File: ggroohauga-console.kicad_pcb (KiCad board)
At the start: 2 copper layers, 95 x 31 mm, 7 parts

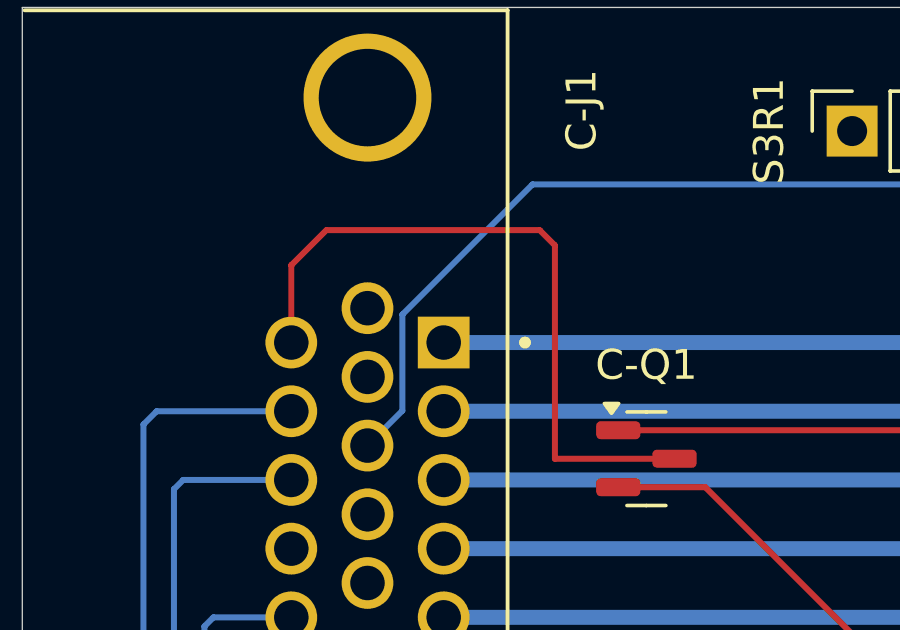
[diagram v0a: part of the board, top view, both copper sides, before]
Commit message: Add 3D models of the DE-15 connectors and realign some tracks
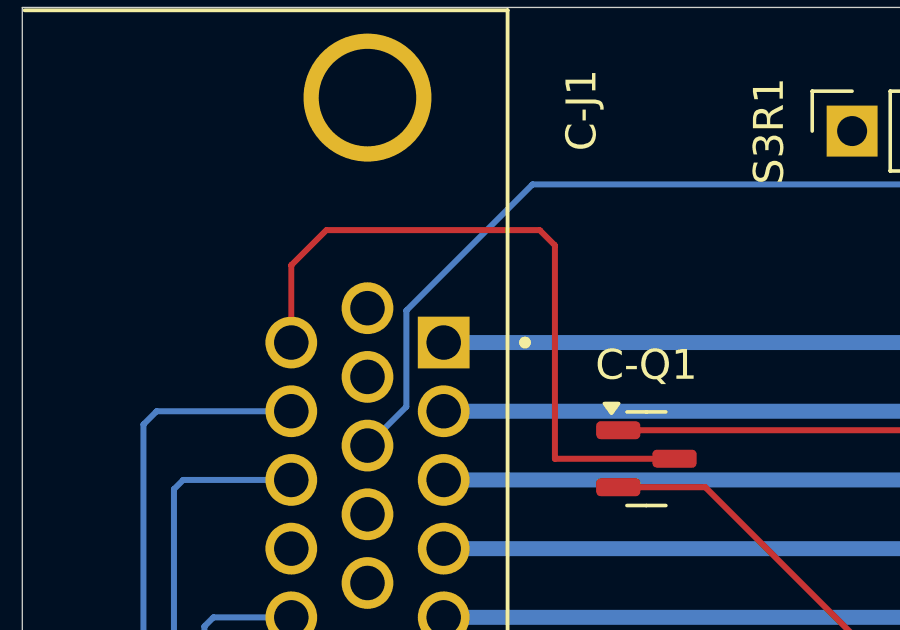
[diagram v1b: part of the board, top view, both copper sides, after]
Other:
- board text added: "urn:oid:1.3.6.1.4.1.39777.1.3.1.2.4"
- board text removed: "urn:oid:1.3.6.1.4.1.39777.1.3.1.2.3"
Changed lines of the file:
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@@
 		)
 		(embedded_fonts no)
+		(model "${KIPRJMOD}/vendor/amphenol/L717HDE15PD1CH4F.step"
+			(offset
+				(xyz 0 -8.5 6.25)
+			)
+			(scale
+				(xyz 1 1 1)
+			)
+			(rotate
+				(xyz -180 -0 -0)
+			)
+		)
 	)
 	(footprint "Connector_PinSocket_2.54mm:PinSocket_1x20_P2.54mm_Vertical"
@@
 		)
 	)
-	(gr_text "urn:oid:1.3.6.1.4.1.39777.1.3.1.2.3"
+	(gr_text "urn:oid:1.3.6.1.4.1.39777.1.3.1.2.4"
 		(at 131.064 56.642 0)
 		(layer "B.SilkS")
@@
 	)
 	(segment
-		(start 120.396 56.388)
-		(end 122.174 54.61)
+		(start 66.675 60.59325)
+		(end 70.88025 56.388)
 		(width 0.2)
 		(layer "B.Cu")
@@
 	)
 	(segment
-		(start 66.5421 63.9317)
-		(end 66.5421 60.72615)
+		(start 66.675 63.7988)
+		(end 66.675 60.59325)
 		(width 0.2)
 		(layer "B.Cu")
@@
 	)
 	(segment
-		(start 65.3796 65.0942)
-		(end 66.5421 63.9317)
+		(start 120.396 56.388)
+		(end 122.174 54.61)
 		(width 0.2)
 		(layer "B.Cu")
@@
 	)
 	(segment
-		(start 66.5421 60.72615)
-		(end 70.88025 56.388)
+		(start 65.3796 65.0942)
+		(end 66.675 63.7988)
 		(width 0.2)
 		(layer "B.Cu")

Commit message: Indicate active low signals on the schematic
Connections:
- net /Common/GPIO_L13_C47_M26/AMP_ANNOUNCE renamed /Common/~{GPIO_L13_C47_M26/AMP_ANNOUNCE}
- net /Common/GPIO_L17_C17_M8/CON_DETECT renamed /Common/~{GPIO_L17_C17_M8/CON_DETECT}
- net /Common/GPIO_L21_C21_M21/AMP_DETECT renamed /Common/~{GPIO_L21_C21_M21/AMP_DETECT}
- net /Common/GPIO_L40_C40_M41/CON_POWER_OUT renamed /Common/~{GPIO_L40_C40_M41/CON_POWER_OUT}
- net /Common/GPIO_L41_C41_M42/CON_ANNOUNCE renamed /Common/~{GPIO_L41_C41_M42/CON_ANNOUNCE}

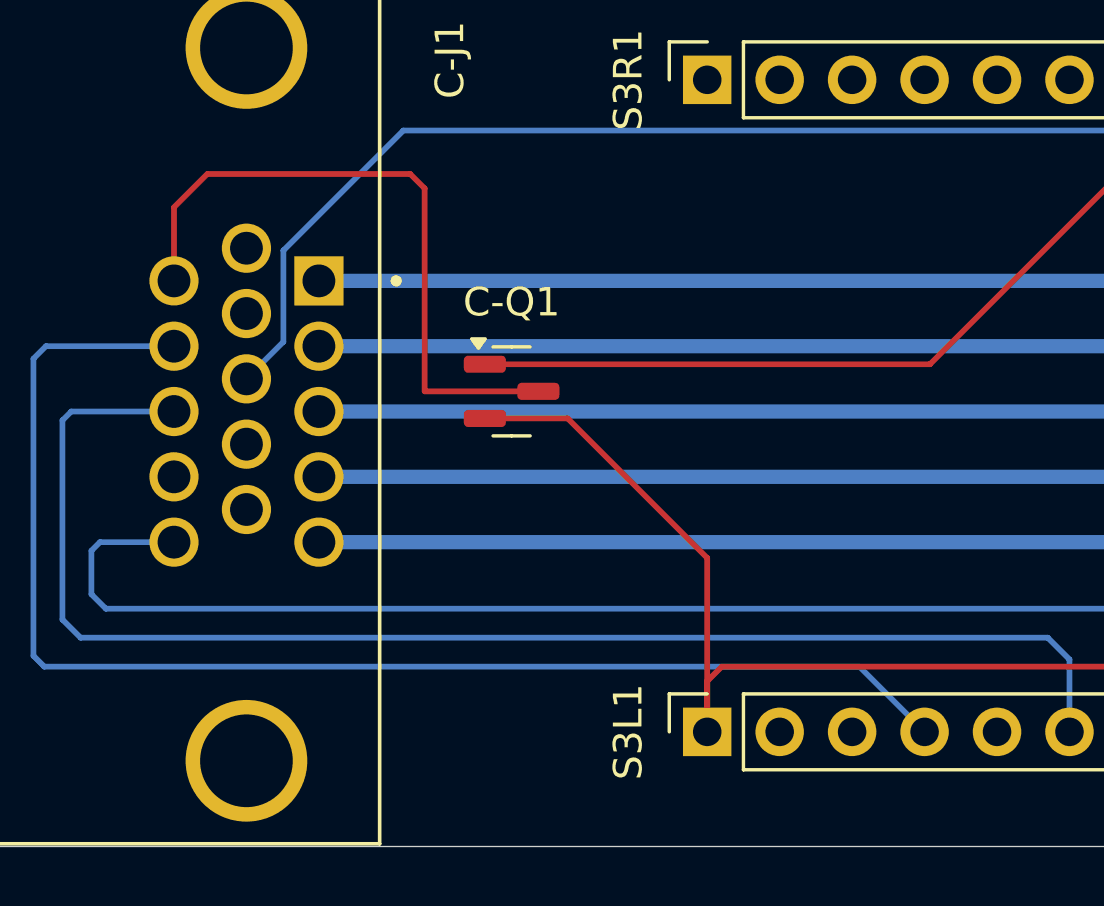
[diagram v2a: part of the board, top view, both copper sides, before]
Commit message: Use the better SOT-23-3 footprint for C-Q1
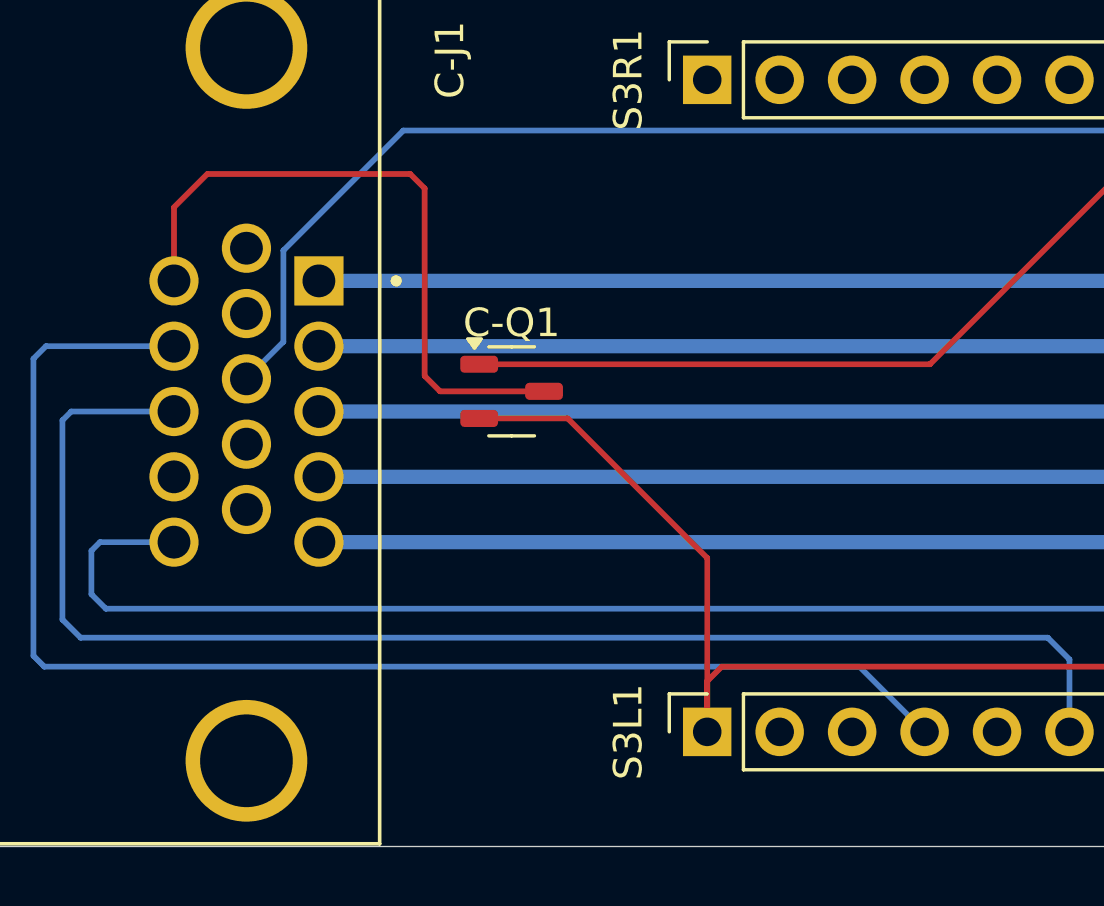
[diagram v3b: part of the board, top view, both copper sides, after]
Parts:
- C-Q1: footprint Package_TO_SOT_SMD:SOT-23 -> Package_TO_SOT_SMD:SOT-23-3
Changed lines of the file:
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@@
 	(net 42 "/Common/~{GPIO_L17_C17_M8{slash}CON_DETECT}")
 	(net 43 "/Common/~{GPIO_L40_C40_M41{slash}CON_POWER_OUT}")
-	(footprint "Package_TO_SOT_SMD:SOT-23"
+	(footprint "Package_TO_SOT_SMD:SOT-23-3"
 		(layer "F.Cu")
 		(at 74.676 65.532)
-		(descr "SOT, 3 Pin (JEDEC TO-236 Var AB https://www.jedec.org/document_search?search_api_views_fulltext=TO-236), generated with kicad-footprint-generator ipc_gullwing_generator.py")
+		(descr "SOT, 3 Pin (JEDEC MO-178 inferred 3-pin variant https://www.jedec.org/document_search?search_api_views_fulltext=MO-178), generated with kicad-footprint-generator ipc_gullwing_generator.py")
 		(tags "SOT TO_SOT_SMD")
 		(property "Reference" "C-Q1"
-			(at 0 -3.1265 0)
+			(at 0 -2.4 0)
 			(layer "F.SilkS")
 			(effects
@@
 		(fp_line
 			(start 0 -1.56)
-			(end -0.65 -1.56)
+			(end -0.8 -1.56)
 			(stroke
 				(width 0.12)
@@
 		(fp_line
 			(start 0 -1.56)
-			(end 0.65 -1.56)
+			(end 0.8 -1.56)
 			(stroke
 				(width 0.12)
@@
 		(fp_line
 			(start 0 1.56)
-			(end -0.65 1.56)
+			(end -0.8 1.56)
 			(stroke
 				(width 0.12)
@@
 		(fp_line
 			(start 0 1.56)
-			(end 0.65 1.56)
+			(end 0.8 1.56)
 			(stroke
 				(width 0.12)
@@
 		(fp_poly
 			(pts
-				(xy -1.1625 -1.51) (xy -1.4025 -1.84) (xy -0.9225 -1.84)
+				(xy -1.3 -1.51) (xy -1.54 -1.84) (xy -1.06 -1.84)
 			)
 			(stroke
@@
 		)
 		(fp_line
-			(start -1.93 -1.5)
-			(end -0.9 -1.5)
+			(start -2.05 -1.5)
+			(end -1.05 -1.5)
 			(stroke
 				(width 0.05)
@@
 		)
 		(fp_line
-			(start -1.93 1.5)
-			(end -1.93 -1.5)
+			(start -2.05 1.5)
+			(end -2.05 -1.5)
 			(stroke
 				(width 0.05)
@@
 		)
 		(fp_line
-			(start -0.9 -1.7)
-			(end 0.9 -1.7)
+			(start -1.05 -1.7)
+			(end 1.05 -1.7)
 			(stroke
 				(width 0.05)
@@
 		)
 		(fp_line
-			(start -0.9 -1.5)
-			(end -0.9 -1.7)
+			(start -1.05 -1.5)
+			(end -1.05 -1.7)
 			(stroke
 				(width 0.05)
@@
 		)
 		(fp_line
-			(start -0.9 1.5)
-			(end -1.93 1.5)
+			(start -1.05 1.5)
+			(end -2.05 1.5)
 			(stroke
 				(width 0.05)
@@
 		)
 		(fp_line
-			(start -0.9 1.7)
-			(end -0.9 1.5)
+			(start -1.05 1.7)
+			(end -1.05 1.5)
 			(stroke
 				(width 0.05)
@@
 		)
 		(fp_line
-			(start 0.9 -1.7)
-			(end 0.9 -0.55)
+			(start 1.05 -1.7)
+			(end 1.05 -0.55)
 			(stroke
 				(width 0.05)
@@
 		)
 		(fp_line
-			(start 0.9 -0.55)
-			(end 1.93 -0.55)
+			(start 1.05 -0.55)
+			(end 2.05 -0.55)
 			(stroke
 				(width 0.05)
@@
 		)
 		(fp_line
-			(start 0.9 0.55)
-			(end 0.9 1.7)
+			(start 1.05 0.55)
+			(end 1.05 1.7)
 			(stroke
 				(width 0.05)
@@
 		)
 		(fp_line
-			(start 0.9 1.7)
-			(end -0.9 1.7)
+			(start 1.05 1.7)
+			(end -1.05 1.7)
 			(stroke
 				(width 0.05)
@@
 		)
 		(fp_line
-			(start 1.93 -0.55)
-			(end 1.93 0.55)
+			(start 2.05 -0.55)
+			(end 2.05 0.55)
 			(stroke
 				(width 0.05)
@@
 		)
 		(fp_line
-			(start 1.93 0.55)
-			(end 0.9 0.55)
+			(start 2.05 0.55)
+			(end 1.05 0.55)
 			(stroke
 				(width 0.05)
@@
 		)
 		(fp_line
-			(start -0.65 -1.125)
-			(end -0.325 -1.45)
+			(start -0.8 -1.05)
+			(end -0.4 -1.45)
 			(stroke
 				(width 0.1)
@@
 		)
 		(fp_line
-			(start -0.65 1.45)
-			(end -0.65 -1.125)
+			(start -0.8 1.45)
+			(end -0.8 -1.05)
 			(stroke
 				(width 0.1)
@@
 		)
 		(fp_line
-			(start -0.325 -1.45)
-			(end 0.65 -1.45)
+			(start -0.4 -1.45)
+			(end 0.8 -1.45)
 			(stroke
 				(width 0.1)
@@
 		)
 		(fp_line
-			(start 0.65 -1.45)
-			(end 0.65 1.45)
+			(start 0.8 -1.45)
+			(end 0.8 1.45)
 			(stroke
 				(width 0.1)
@@
 		)
 		(fp_line
-			(start 0.65 1.45)
-			(end -0.65 1.45)
+			(start 0.8 1.45)
+			(end -0.8 1.45)
 			(stroke
 				(width 0.1)
@@
 			(effects
 				(font
-					(size 0.32 0.32)
-					(thickness 0.05)
+					(size 0.4 0.4)
+					(thickness 0.06)
 				)
 			)
 		)
 		(pad "1" smd roundrect
-			(at -0.9375 -0.95)
-			(size 1.475 0.6)
+			(at -1.1375 -0.95)
+			(size 1.325 0.6)
 			(layers "F.Cu" "F.Mask" "F.Paste")
 			(roundrect_rratio 0.25)
@@
 		)
 		(pad "2" smd roundrect
-			(at -0.9375 0.95)
-			(size 1.475 0.6)
+			(at -1.1375 0.95)
+			(size 1.325 0.6)
 			(layers "F.Cu" "F.Mask" "F.Paste")
 			(roundrect_rratio 0.25)
@@
 		)
 		(pad "3" smd roundrect
-			(at 0.9375 0)
-			(size 1.475 0.6)
+			(at 1.1375 0)
+			(size 1.325 0.6)
 			(layers "F.Cu" "F.Mask" "F.Paste")
 			(roundrect_rratio 0.25)
@@
 		)
 		(embedded_fonts no)
-		(model "${KICAD9_3DMODEL_DIR}/Package_TO_SOT_SMD.3dshapes/SOT-23.step"
+		(model "${KICAD9_3DMODEL_DIR}/Package_TO_SOT_SMD.3dshapes/SOT-23-3.step"
 			(offset
 				(xyz 0 0 0)
@@
 	)
 	(segment
+		(start 73.5385 66.482)
+		(end 76.642 66.482)
+		(width 0.2)
+		(layer "F.Cu")
+		(net 8)
+	)
+	(segment
 		(start 76.642 66.482)
 		(end 81.534 71.374)
@@
 	)
 	(segment
-		(start 81.534 77.47)
-		(end 81.534 71.374)
-		(width 0.2)
-		(layer "F.Cu")
-		(net 8)
-	)
-	(segment
-		(start 73.7385 66.482)
-		(end 76.642 66.482)
+		(start 82.042 75.184)
+		(end 81.534 75.692)
 		(width 0.2)
 		(layer "F.Cu")
@@
 	)
 	(segment
-		(start 82.042 75.184)
-		(end 81.534 75.692)
+		(start 81.534 75.692)
+		(end 81.534 77.47)
 		(width 0.2)
 		(layer "F.Cu")
@@
 	)
 	(segment
-		(start 81.534 75.692)
+		(start 81.534 71.374)
 		(end 81.534 77.47)
 		(width 0.2)
@@
 	)
 	(segment
-		(start 75.6135 65.532)
-		(end 71.628 65.532)
+		(start 71.12 57.912)
+		(end 64.008 57.912)
 		(width 0.2)
 		(layer "F.Cu")
@@
 	)
 	(segment
-		(start 71.628 58.42)
-		(end 71.12 57.912)
+		(start 75.8135 65.532)
+		(end 72.16775 65.532)
 		(width 0.2)
 		(layer "F.Cu")
@@
 	)
 	(segment
-		(start 62.8396 59.0804)
-		(end 64.008 57.912)
+		(start 71.628 64.99225)
+		(end 71.628 58.42)
 		(width 0.2)
 		(layer "F.Cu")
@@
 	)
 	(segment
-		(start 71.628 65.532)
-		(end 71.628 58.42)
+		(start 72.16775 65.532)
+		(end 71.628 64.99225)
 		(width 0.2)
 		(layer "F.Cu")
@@
 	)
 	(segment
-		(start 62.8396 61.6592)
-		(end 62.8396 59.0804)
+		(start 71.628 58.42)
+		(end 71.12 57.912)
+		(width 0.2)
+		(layer "F.Cu")
+		(net 33)
+	)
+	(segment
+		(start 62.8396 59.0804)
+		(end 62.8396 61.6592)
 		(width 0.2)
 		(layer "F.Cu")
@@
 	(segment
 		(start 64.008 57.912)
-		(end 71.12 57.912)
+		(end 62.8396 59.0804)
 		(width 0.2)
 		(layer "F.Cu")
@@
 	)
 	(segment
-		(start 73.7385 64.582)
+		(start 73.5385 64.582)
 		(end 89.342 64.582)
 		(width 0.2)

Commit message: Use shorter PCB URLs
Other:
- board text added: "https://pcb.nom.is/ggroohauga (console)"
- board text removed: "https://github.com/nomis/ggroohauga-pcb (console)"
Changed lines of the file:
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@@
 		)
 	)
-	(gr_text "https://github.com/nomis/ggroohauga-pcb (console)"
+	(gr_text "https://pcb.nom.is/ggroohauga (console)"
 		(at 131.064 73.533 0)
 		(layer "B.SilkS")
